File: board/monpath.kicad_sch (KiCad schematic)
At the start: 120 parts, among them J2 BEL_FUSE_0826-1G1T-23-F, J8 BEL_FUSE_0826-1G1T-23-F, U10 ECS-2016MVQ-250-CN-TR, U11 ECS-2016MVQ-250-CN-TR, U12 ECS-2016MVQ-250-CN-TR, U2 KSZ9031RN, U4 XC7S15-1FTGB196C, U9 KSZ9031RN

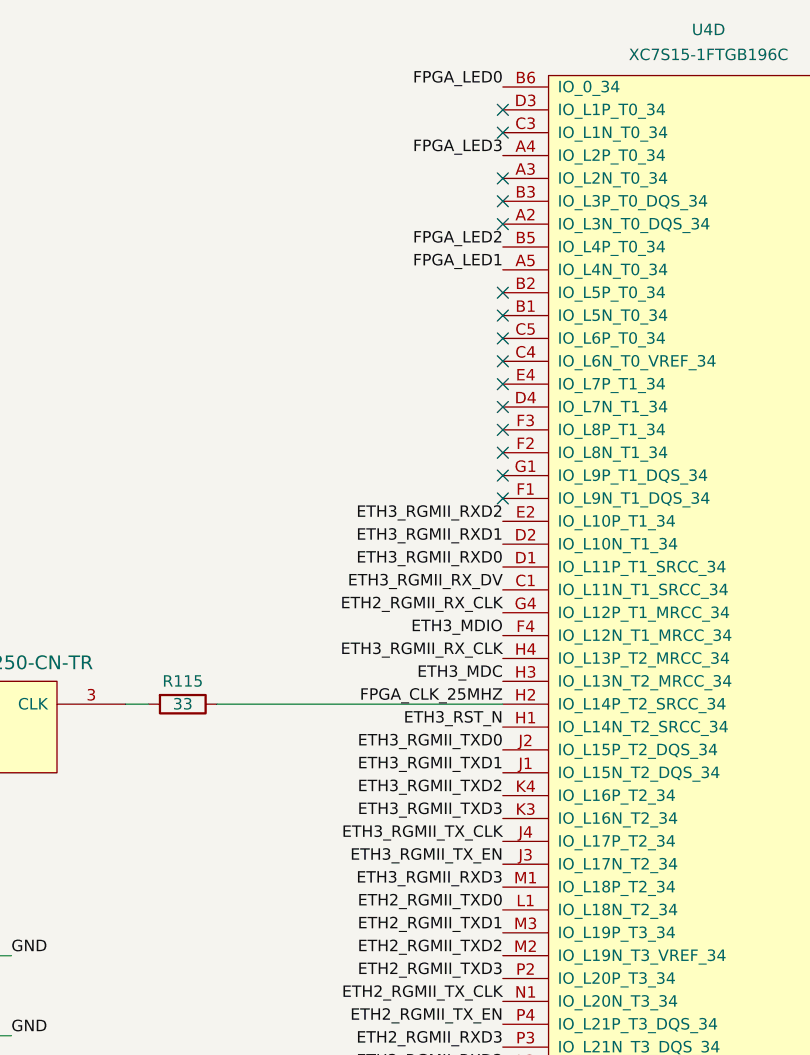
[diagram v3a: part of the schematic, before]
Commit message: Finished power supply layout, added mounting holes and a bunch of silkscreen labeling
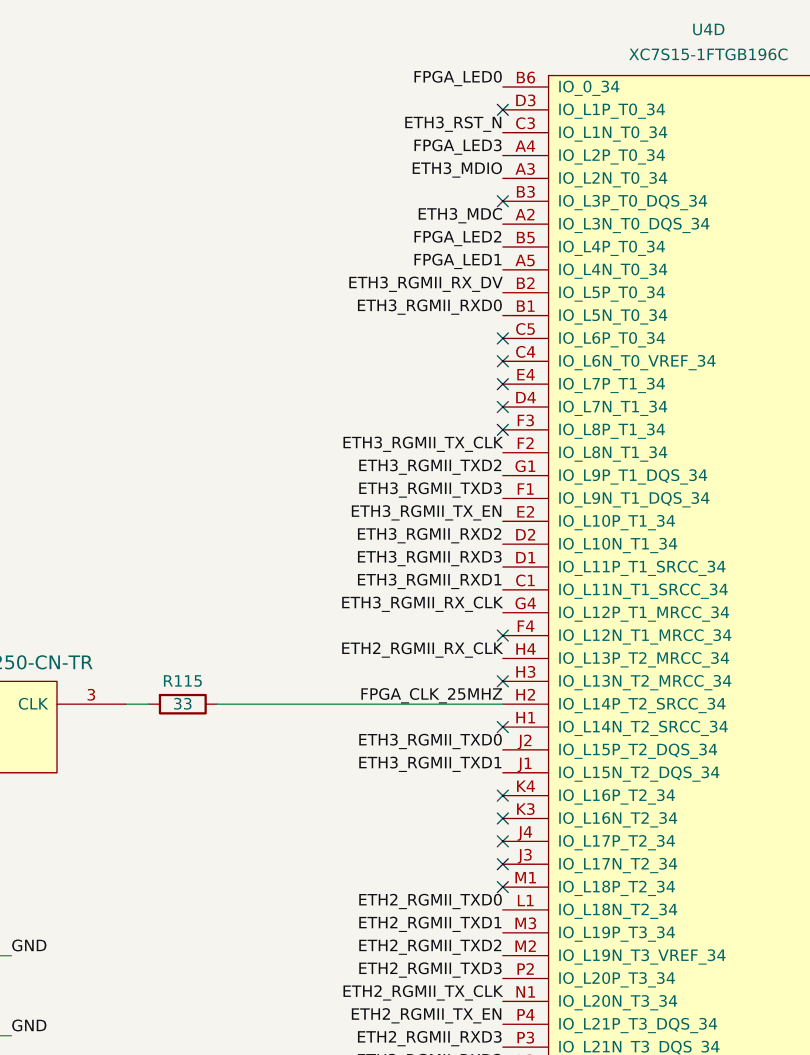
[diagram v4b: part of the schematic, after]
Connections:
- net ETH2_RGMII_RX_CLK: now also U4.H4 (IO_L13P_T2_MRCC_34); no longer U4.G4 (IO_L12P_T1_MRCC_34)
- net ETH3_MDC: now also U4.A2 (IO_L3N_T0_DQS_34); no longer U4.H3 (IO_L13N_T2_MRCC_34)
- net ETH3_MDIO: now also U4.A3 (IO_L2N_T0_34); no longer U4.F4 (IO_L12N_T1_MRCC_34)
- net ETH3_RGMII_RXD0: now also U4.B1 (IO_L5N_T0_34); no longer U4.D1 (IO_L11P_T1_SRCC_34)
- net ETH3_RGMII_RXD1: now also U4.C1 (IO_L11N_T1_SRCC_34); no longer U4.D2 (IO_L10N_T1_34)
- net ETH3_RGMII_RXD2: now also U4.D2 (IO_L10N_T1_34); no longer U4.E2 (IO_L10P_T1_34)
- net ETH3_RGMII_RXD3: now also U4.D1 (IO_L11P_T1_SRCC_34); no longer U4.M1 (IO_L18P_T2_34)
- net ETH3_RGMII_RX_CLK: now also U4.G4 (IO_L12P_T1_MRCC_34); no longer U4.H4 (IO_L13P_T2_MRCC_34)
- net ETH3_RGMII_RX_DV: now also U4.B2 (IO_L5P_T0_34); no longer U4.C1 (IO_L11N_T1_SRCC_34)
- net ETH3_RGMII_TXD2: now also U4.G1 (IO_L9P_T1_DQS_34); no longer U4.K4 (IO_L16P_T2_34)
- net ETH3_RGMII_TXD3: now also U4.F1 (IO_L9N_T1_DQS_34); no longer U4.K3 (IO_L16N_T2_34)
- net ETH3_RGMII_TX_CLK: now also U4.F2 (IO_L8N_T1_34); no longer U4.J4 (IO_L17P_T2_34)
- net ETH3_RGMII_TX_EN: now also U4.E2 (IO_L10P_T1_34); no longer U4.J3 (IO_L17N_T2_34)
- net ETH3_RST_N: now also U4.C3 (IO_L1N_T0_34); no longer U4.H1 (IO_L14N_T2_SRCC_34)
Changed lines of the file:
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@@
   (title_block
     (title "Active 10/100/1000baseT Tap")
-    (date "2022-12-21")
+    (date "2022-12-23")
     (rev "0.1")
     (company "Antikernel Labs")
@@
   )
   (no_connect (at 365.76 50.8))
-  (no_connect (at 365.76 45.72))
-  (no_connect (at 365.76 66.04))
-  (no_connect (at 365.76 48.26))
+  (no_connect (at 365.76 111.76))
   (no_connect (at 365.76 35.56))
   (no_connect (at 95.25 72.39))
   (no_connect (at 365.76 53.34))
+  (no_connect (at 365.76 93.98))
   (no_connect (at 152.4 80.01))
+  (no_connect (at 365.76 109.22))
+  (no_connect (at 365.76 101.6))
   (no_connect (at 365.76 55.88))
-  (no_connect (at 365.76 63.5))
+  (no_connect (at 365.76 83.82))
+  (no_connect (at 365.76 88.9))
+  (no_connect (at 365.76 106.68))
   (no_connect (at 95.25 161.29))
   (no_connect (at 365.76 25.4))
@@
   (no_connect (at 152.4 91.44))
   (no_connect (at 365.76 60.96))
-  (no_connect (at 365.76 27.94))
-  (no_connect (at 365.76 68.58))
-  (no_connect (at 365.76 38.1))
+  (no_connect (at 365.76 104.14))
   (no_connect (at 365.76 58.42))
   (no_connect (at 152.4 168.91))
-  (no_connect (at 365.76 33.02))
   (wire (pts (xy 48.26 128.27) (xy 59.69 128.27))
     (stroke (width 0) (type default) (color 0 0 0 0))
@@
     (effects (font (size 1.27 1.27)) (justify right bottom))
   )
-  (label "ETH3_RGMII_TXD3" (at 365.76 104.14 180)
+  (label "ETH3_RGMII_TXD3" (at 365.76 68.58 180)
     (effects (font (size 1.27 1.27)) (justify right bottom))
   )
@@
     (effects (font (size 1.27 1.27)) (justify right bottom))
   )
-  (label "ETH3_RGMII_RXD3" (at 365.76 111.76 180)
+  (label "ETH3_RGMII_RXD3" (at 365.76 76.2 180)
     (effects (font (size 1.27 1.27)) (justify right bottom))
   )
@@
     (effects (font (size 1.27 1.27)) (justify left bottom))
   )
-  (label "ETH3_RGMII_TX_CLK" (at 365.76 106.68 180)
+  (label "ETH3_RGMII_TX_CLK" (at 365.76 63.5 180)
     (effects (font (size 1.27 1.27)) (justify right bottom))
   )
@@
     (effects (font (size 1.27 1.27)) (justify right bottom))
   )
-  (label "ETH3_RGMII_RX_DV" (at 365.76 78.74 180)
+  (label "ETH3_RGMII_RX_DV" (at 365.76 45.72 180)
     (effects (font (size 1.27 1.27)) (justify right bottom))
   )
@@
     (effects (font (size 1.27 1.27)) (justify left bottom))
   )
-  (label "ETH3_RGMII_RX_CLK" (at 365.76 86.36 180)
+  (label "ETH3_RGMII_RX_CLK" (at 365.76 81.28 180)
     (effects (font (size 1.27 1.27)) (justify right bottom))
   )
@@
     (effects (font (size 1.27 1.27)) (justify right bottom))
   )
-  (label "ETH3_MDIO" (at 365.76 83.82 180)
+  (label "ETH3_MDIO" (at 365.76 33.02 180)
     (effects (font (size 1.27 1.27)) (justify right bottom))
   )
@@
     (effects (font (size 1.27 1.27)) (justify right bottom))
   )
-  (label "ETH3_RGMII_RXD0" (at 365.76 76.2 180)
+  (label "ETH3_RGMII_RXD0" (at 365.76 48.26 180)
     (effects (font (size 1.27 1.27)) (justify right bottom))
   )
@@
     (effects (font (size 1.27 1.27)) (justify right bottom))
   )
-  (label "ETH3_RGMII_RXD2" (at 365.76 71.12 180)
-    (effects (font (size 1.27 1.27)) (justify right bottom))
-  )
-  (label "ETH2_RGMII_RX_CLK" (at 365.76 81.28 180)
+  (label "ETH3_RGMII_RXD2" (at 365.76 73.66 180)
+    (effects (font (size 1.27 1.27)) (justify right bottom))
+  )
+  (label "ETH2_RGMII_RX_CLK" (at 365.76 86.36 180)
     (effects (font (size 1.27 1.27)) (justify right bottom))
   )
@@
     (effects (font (size 1.27 1.27)) (justify left bottom))
   )
-  (label "ETH3_RGMII_RXD1" (at 365.76 73.66 180)
+  (label "ETH3_RGMII_RXD1" (at 365.76 78.74 180)
     (effects (font (size 1.27 1.27)) (justify right bottom))
   )
@@
     (effects (font (size 1.27 1.27)) (justify right bottom))
   )
-  (label "ETH3_RST_N" (at 365.76 93.98 180)
+  (label "ETH3_RST_N" (at 365.76 27.94 180)
     (effects (font (size 1.27 1.27)) (justify right bottom))
   )
@@
     (effects (font (size 1.27 1.27)) (justify right bottom))
   )
-  (label "ETH3_MDC" (at 365.76 88.9 180)
+  (label "ETH3_MDC" (at 365.76 38.1 180)
     (effects (font (size 1.27 1.27)) (justify right bottom))
   )
@@
     (effects (font (size 1.27 1.27)) (justify left bottom))
   )
-  (label "ETH3_RGMII_TX_EN" (at 365.76 109.22 180)
+  (label "ETH3_RGMII_TX_EN" (at 365.76 71.12 180)
     (effects (font (size 1.27 1.27)) (justify right bottom))
   )
@@
     (effects (font (size 1.27 1.27)) (justify left bottom))
   )
-  (label "ETH3_RGMII_TXD2" (at 365.76 101.6 180)
-    (effects (font (size 1.27 1.27)) (justify right bottom))
-  )
+  (label "ETH3_RGMII_TXD2" (at 365.76 66.04 180)
+    (effects (font (size 1.27 1.27)) (justify right bottom))
+  )

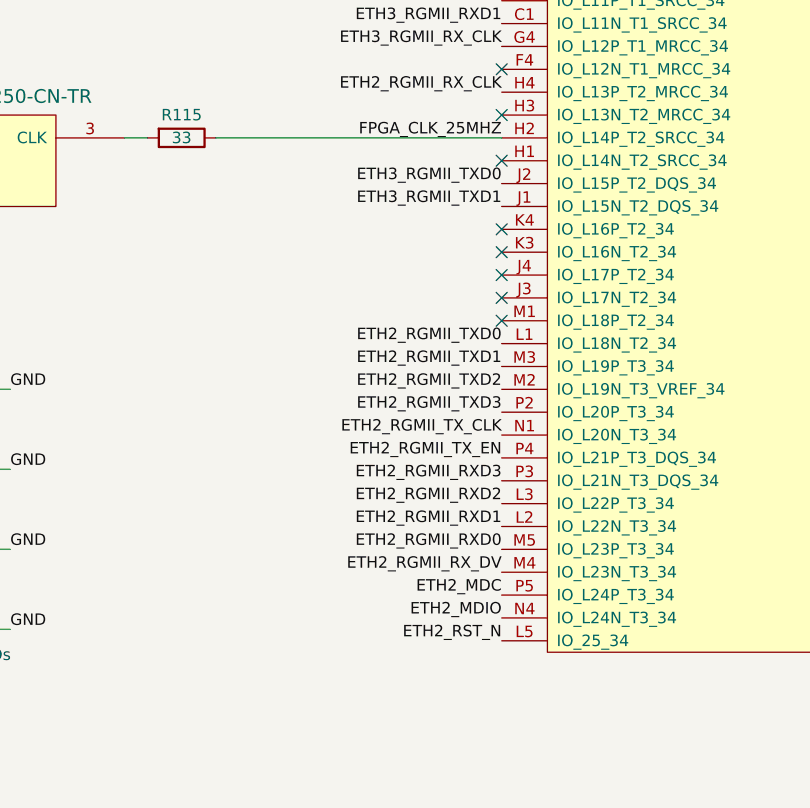
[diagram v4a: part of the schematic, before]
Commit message: Continued work on layout. Monitor port PHys are now done, as is FPGA JTAG and reset
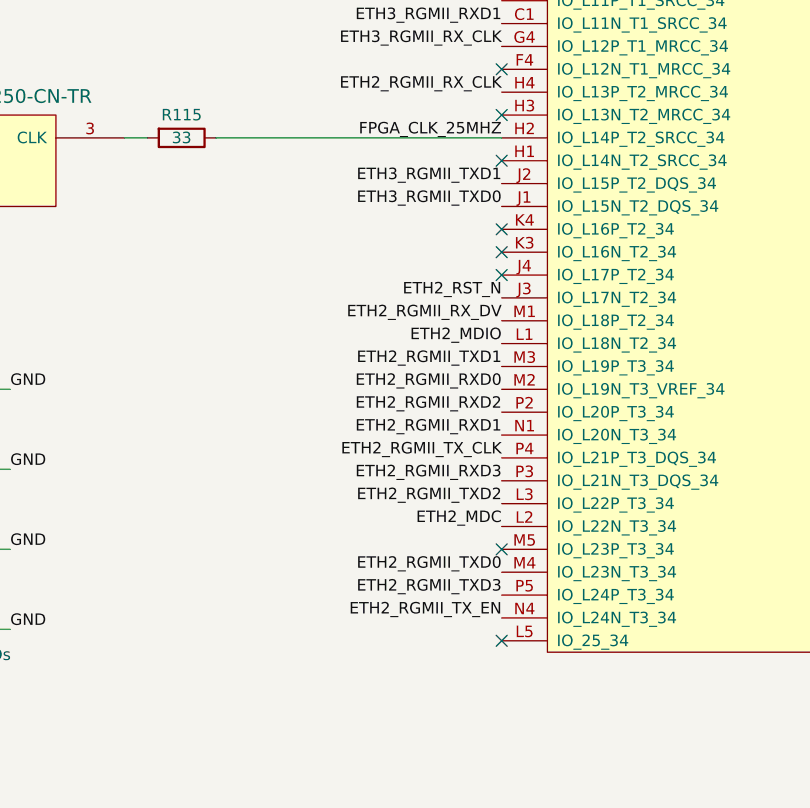
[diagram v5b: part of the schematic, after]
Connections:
- net ETH2_MDC: now also U4.L2 (IO_L22N_T3_34); no longer U4.P5 (IO_L24P_T3_34)
- net ETH2_MDIO: now also U4.L1 (IO_L18N_T2_34); no longer U4.N4 (IO_L24N_T3_34)
- net ETH2_RGMII_RXD0: now also U4.M2 (IO_L19N_T3_VREF_34); no longer U4.M5 (IO_L23P_T3_34)
- net ETH2_RGMII_RXD1: now also U4.N1 (IO_L20N_T3_34); no longer U4.L2 (IO_L22N_T3_34)
- net ETH2_RGMII_RXD2: now also U4.P2 (IO_L20P_T3_34); no longer U4.L3 (IO_L22P_T3_34)
- net ETH2_RGMII_RX_DV: now also U4.M1 (IO_L18P_T2_34); no longer U4.M4 (IO_L23N_T3_34)
- net ETH2_RGMII_TXD0: now also U4.M4 (IO_L23N_T3_34); no longer U4.L1 (IO_L18N_T2_34)
- net ETH2_RGMII_TXD2: now also U4.L3 (IO_L22P_T3_34); no longer U4.M2 (IO_L19N_T3_VREF_34)
- net ETH2_RGMII_TXD3: now also U4.P5 (IO_L24P_T3_34); no longer U4.P2 (IO_L20P_T3_34)
- net ETH2_RGMII_TX_CLK: now also U4.P4 (IO_L21P_T3_DQS_34); no longer U4.N1 (IO_L20N_T3_34)
- net ETH2_RGMII_TX_EN: now also U4.N4 (IO_L24N_T3_34); no longer U4.P4 (IO_L21P_T3_DQS_34)
- net ETH2_RST_N: now also U4.J3 (IO_L17N_T2_34); no longer U4.L5 (IO_25_34)
- net ETH3_RGMII_TXD0: now also U4.J1 (IO_L15N_T2_DQS_34); no longer U4.J2 (IO_L15P_T2_DQS_34)
- net ETH3_RGMII_TXD1: now also U4.J2 (IO_L15P_T2_DQS_34); no longer U4.J1 (IO_L15N_T2_DQS_34)
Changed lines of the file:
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@@
   )
   (no_connect (at 365.76 50.8))
-  (no_connect (at 365.76 111.76))
   (no_connect (at 365.76 35.56))
   (no_connect (at 95.25 72.39))
@@
   (no_connect (at 365.76 93.98))
   (no_connect (at 152.4 80.01))
-  (no_connect (at 365.76 109.22))
   (no_connect (at 365.76 101.6))
   (no_connect (at 365.76 55.88))
@@
   (no_connect (at 95.25 161.29))
   (no_connect (at 365.76 25.4))
+  (no_connect (at 365.76 137.16))
   (no_connect (at 152.4 180.34))
   (no_connect (at 152.4 91.44))
   (no_connect (at 365.76 60.96))
   (no_connect (at 365.76 104.14))
+  (no_connect (at 365.76 147.32))
   (no_connect (at 365.76 58.42))
   (no_connect (at 152.4 168.91))
@@
     (effects (font (size 1.27 1.27)) (justify left bottom))
   )
-  (label "ETH2_RGMII_TXD2" (at 365.76 119.38 180)
+  (label "ETH2_RGMII_TXD2" (at 365.76 132.08 180)
     (effects (font (size 1.27 1.27)) (justify right bottom))
   )
@@
     (effects (font (size 1.27 1.27)) (justify right bottom))
   )
-  (label "ETH2_RGMII_TXD3" (at 365.76 121.92 180)
+  (label "ETH2_RGMII_TXD3" (at 365.76 142.24 180)
     (effects (font (size 1.27 1.27)) (justify right bottom))
   )
@@
     (effects (font (size 1.27 1.27)) (justify right bottom))
   )
-  (label "ETH2_RGMII_TX_EN" (at 365.76 127 180)
+  (label "ETH2_RGMII_TX_EN" (at 365.76 144.78 180)
     (effects (font (size 1.27 1.27)) (justify right bottom))
   )
@@
     (effects (font (size 1.27 1.27)) (justify right bottom))
   )
-  (label "ETH2_RGMII_RXD0" (at 365.76 137.16 180)
+  (label "ETH2_RGMII_RXD0" (at 365.76 119.38 180)
     (effects (font (size 1.27 1.27)) (justify right bottom))
   )
@@
     (effects (font (size 1.27 1.27)) (justify right bottom))
   )
-  (label "ETH2_RGMII_TX_CLK" (at 365.76 124.46 180)
+  (label "ETH2_RGMII_TX_CLK" (at 365.76 127 180)
     (effects (font (size 1.27 1.27)) (justify right bottom))
   )
@@
     (effects (font (size 1.27 1.27)) (justify right bottom))
   )
-  (label "ETH2_RST_N" (at 365.76 147.32 180)
+  (label "ETH2_RST_N" (at 365.76 109.22 180)
     (effects (font (size 1.27 1.27)) (justify right bottom))
   )
@@
     (effects (font (size 1.27 1.27)) (justify right bottom))
   )
-  (label "ETH2_MDIO" (at 365.76 144.78 180)
-    (effects (font (size 1.27 1.27)) (justify right bottom))
-  )
-  (label "ETH2_MDC" (at 365.76 142.24 180)
+  (label "ETH2_MDIO" (at 365.76 114.3 180)
+    (effects (font (size 1.27 1.27)) (justify right bottom))
+  )
+  (label "ETH2_MDC" (at 365.76 134.62 180)
     (effects (font (size 1.27 1.27)) (justify right bottom))
   )
@@
     (effects (font (size 1.27 1.27)) (justify left bottom))
   )
-  (label "ETH3_RGMII_TXD0" (at 365.76 96.52 180)
+  (label "ETH3_RGMII_TXD0" (at 365.76 99.06 180)
     (effects (font (size 1.27 1.27)) (justify right bottom))
   )
@@
     (effects (font (size 1.27 1.27)) (justify right bottom))
   )
-  (label "ETH2_RGMII_TXD0" (at 365.76 114.3 180)
+  (label "ETH2_RGMII_TXD0" (at 365.76 139.7 180)
     (effects (font (size 1.27 1.27)) (justify right bottom))
   )
@@
     (effects (font (size 1.27 1.27)) (justify left bottom))
   )
-  (label "ETH3_RGMII_TXD1" (at 365.76 99.06 180)
+  (label "ETH3_RGMII_TXD1" (at 365.76 96.52 180)
     (effects (font (size 1.27 1.27)) (justify right bottom))
   )
@@
     (effects (font (size 1.27 1.27)) (justify left bottom))
   )
-  (label "ETH2_RGMII_RXD2" (at 365.76 132.08 180)
+  (label "ETH2_RGMII_RXD2" (at 365.76 121.92 180)
     (effects (font (size 1.27 1.27)) (justify right bottom))
   )
@@
     (effects (font (size 1.27 1.27)) (justify left bottom))
   )
-  (label "ETH2_RGMII_RXD1" (at 365.76 134.62 180)
+  (label "ETH2_RGMII_RXD1" (at 365.76 124.46 180)
     (effects (font (size 1.27 1.27)) (justify right bottom))
   )
@@
     (effects (font (size 1.27 1.27)) (justify left bottom))
   )
-  (label "ETH2_RGMII_RX_DV" (at 365.76 139.7 180)
-    (effects (font (size 1.27 1.27)) (justify right bottom))
-  )
+  (label "ETH2_RGMII_RX_DV" (at 365.76 111.76 180)
+    (effects (font (size 1.27 1.27)) (justify right bottom))
+  )

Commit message: Final v0.1 layout after design review
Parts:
- added C185, C186: 0.47 uF, azonenberg_pcb:EIA_0402_CAP_NOSILK, symbol device:C
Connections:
- net 3V3: now also C185.1, C186.1
- net GND: now also C185.2, C186.2
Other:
- note added: "Stitching caps for ref plane changes"
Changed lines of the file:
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@@
   (title_block
     (title "Active 10/100/1000baseT Tap")
-    (date "2022-12-26")
+    (date "2022-12-27")
     (rev "0.1")
     (company "Antikernel Labs")
@@
     (stroke (width 0) (type default) (color 0 0 0 0))
   )
+  (wire (pts (xy 288.29 195.58) (xy 302.26 195.58))
+    (stroke (width 0) (type default) (color 0 0 0 0))
+  )
   (wire (pts (xy 326.39 91.44) (xy 323.85 91.44))
     (stroke (width 0) (type default) (color 0 0 0 0))
@@
     (stroke (width 0) (type default) (color 0 0 0 0))
   )
+  (wire (pts (xy 288.29 187.96) (xy 302.26 187.96))
+    (stroke (width 0) (type default) (color 0 0 0 0))
+  )
   (wire (pts (xy 337.82 240.03) (xy 335.28 240.03))
     (stroke (width 0) (type default) (color 0 0 0 0))
@@
     (effects (font (size 1.27 1.27)) (justify left bottom))
   )
+  (text "Stitching caps for ref plane changes" (at 288.29 198.12 0)
+    (effects (font (size 1.27 1.27)) (justify left bottom))
+  )
   (text "Strap: advertise everything but gig/half" (at 213.36 53.34 0)
     (effects (font (size 1.27 1.27)) (justify left bottom))
@@
     (effects (font (size 1.27 1.27)) (justify left bottom))
   )
+  (label "3V3" (at 288.29 187.96 180)
+    (effects (font (size 1.27 1.27)) (justify right bottom))
+  )
   (label "ETH2_RGMII_TXD2" (at 365.76 132.08 180)
     (effects (font (size 1.27 1.27)) (justify right bottom))
@@
   (label "GND" (at 63.5 77.47 0)
     (effects (font (size 1.27 1.27)) (justify left bottom))
+  )
+  (label "GND" (at 288.29 195.58 180)
+    (effects (font (size 1.27 1.27)) (justify right bottom))
   )
   (label "ETH3_LED1_N" (at 176.53 124.46 0)
@@
     (pin "2")
   )
+  (symbol (lib_id "device:C") (at 288.29 191.77 0) (unit 1)
+    (in_bom yes) (on_board yes)
+    (property "Reference" "C185" (id 0) (at 291.211 190.6016 0)
+      (effects (font (size 1.27 1.27)) (justify left))
+    )
+    (property "Value" "0.47 uF" (id 1) (at 291.211 192.913 0)
+      (effects (font (size 1.27 1.27)) (justify left))
+    )
+    (property "Footprint" "azonenberg_pcb:EIA_0402_CAP_NOSILK" (id 2) (at 289.2552 195.58 0)
+      (effects (font (size 1.27 1.27)) hide)
+    )
+    (property "Datasheet" "" (id 3) (at 288.29 191.77 0)
+      (effects (font (size 1.27 1.27)) hide)
+    )
+    (pin "1")
+    (pin "2")
+  )
   (symbol (lib_id "passive-azonenberg:FERRITE_SMALL2") (at 220.98 210.82 0) (unit 1)
     (in_bom yes) (on_board yes)
@@
     )
     (pin "1")
+    (pin "2")
+  )
+  (symbol (lib_id "device:C") (at 302.26 191.77 0) (unit 1)
+    (in_bom yes) (on_board yes)
+    (property "Reference" "C186" (id 0) (at 305.181 190.6016 0)
+      (effects (font (size 1.27 1.27)) (justify left))
+    )
+    (property "Value" "0.47 uF" (id 1) (at 305.181 192.913 0)
+      (effects (font (size 1.27 1.27)) (justify left))
+    )
+    (property "Footprint" "azonenberg_pcb:EIA_0402_CAP_NOSILK" (id 2) (at 303.2252 195.58 0)
+      (effects (font (size 1.27 1.27)) hide)
+    )
+    (property "Datasheet" "" (id 3) (at 302.26 191.77 0)
+      (effects (font (size 1.27 1.27)) hide)
+    )
+    (pin "1")
